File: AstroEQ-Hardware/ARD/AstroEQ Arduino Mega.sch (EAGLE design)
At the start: 19 parts, among them J1 POWER_JACKPTH, M0 Motor Driver, M1 Motor Driver

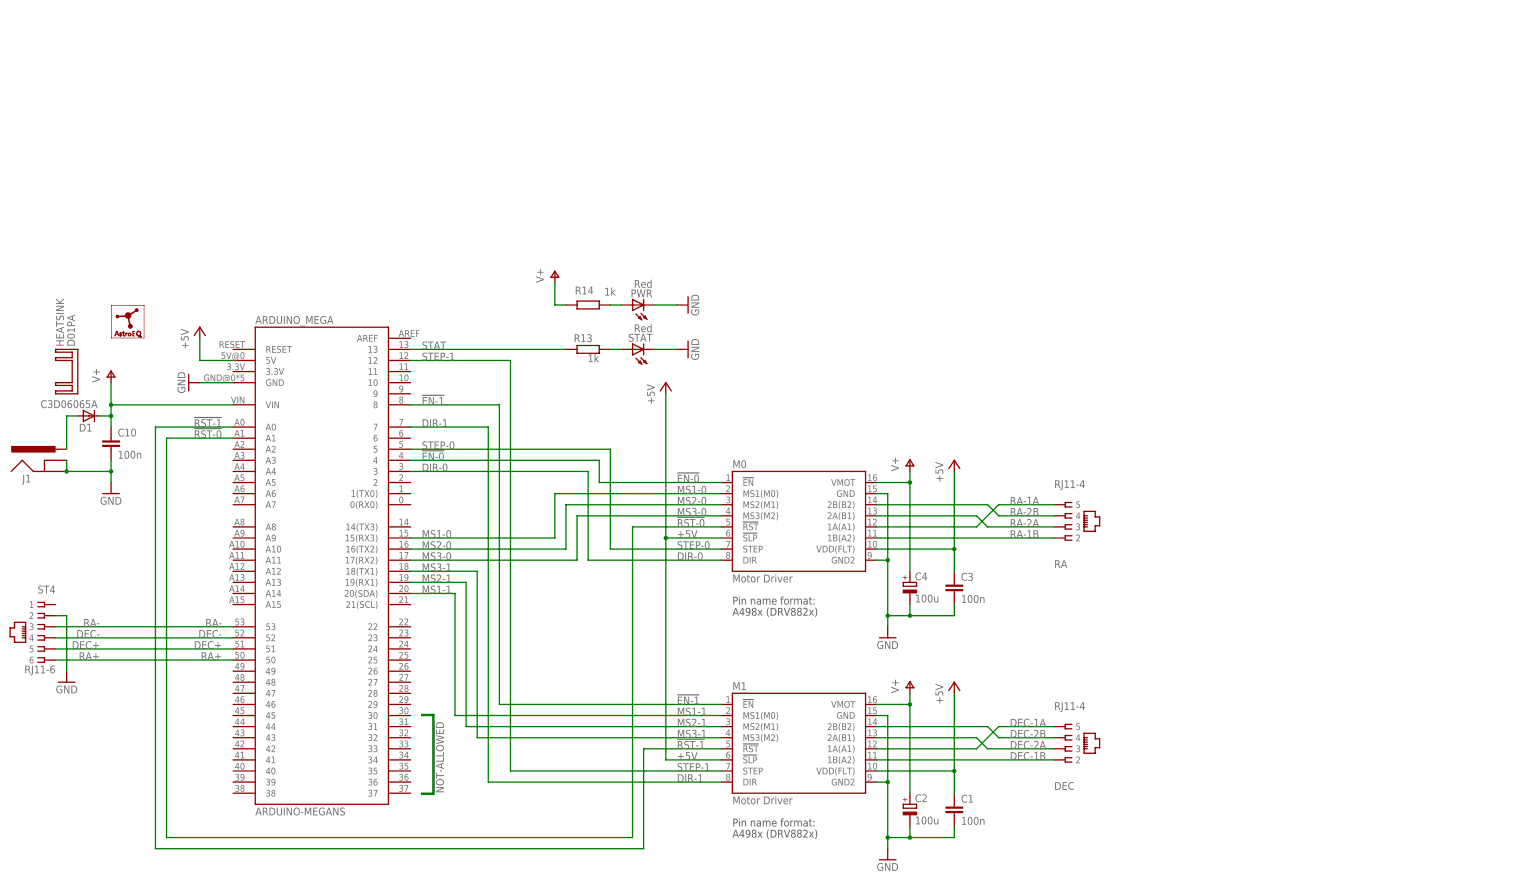
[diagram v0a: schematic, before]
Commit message: Update Arduino Mega PCB design to V4.8
Adds:
* Speed control line to ST4 connector
* DRV8834 support using 3-pin jumper selection headers.
* PWM output connector jack
* IO header for target speed selection, emergency stop, and snap pin.
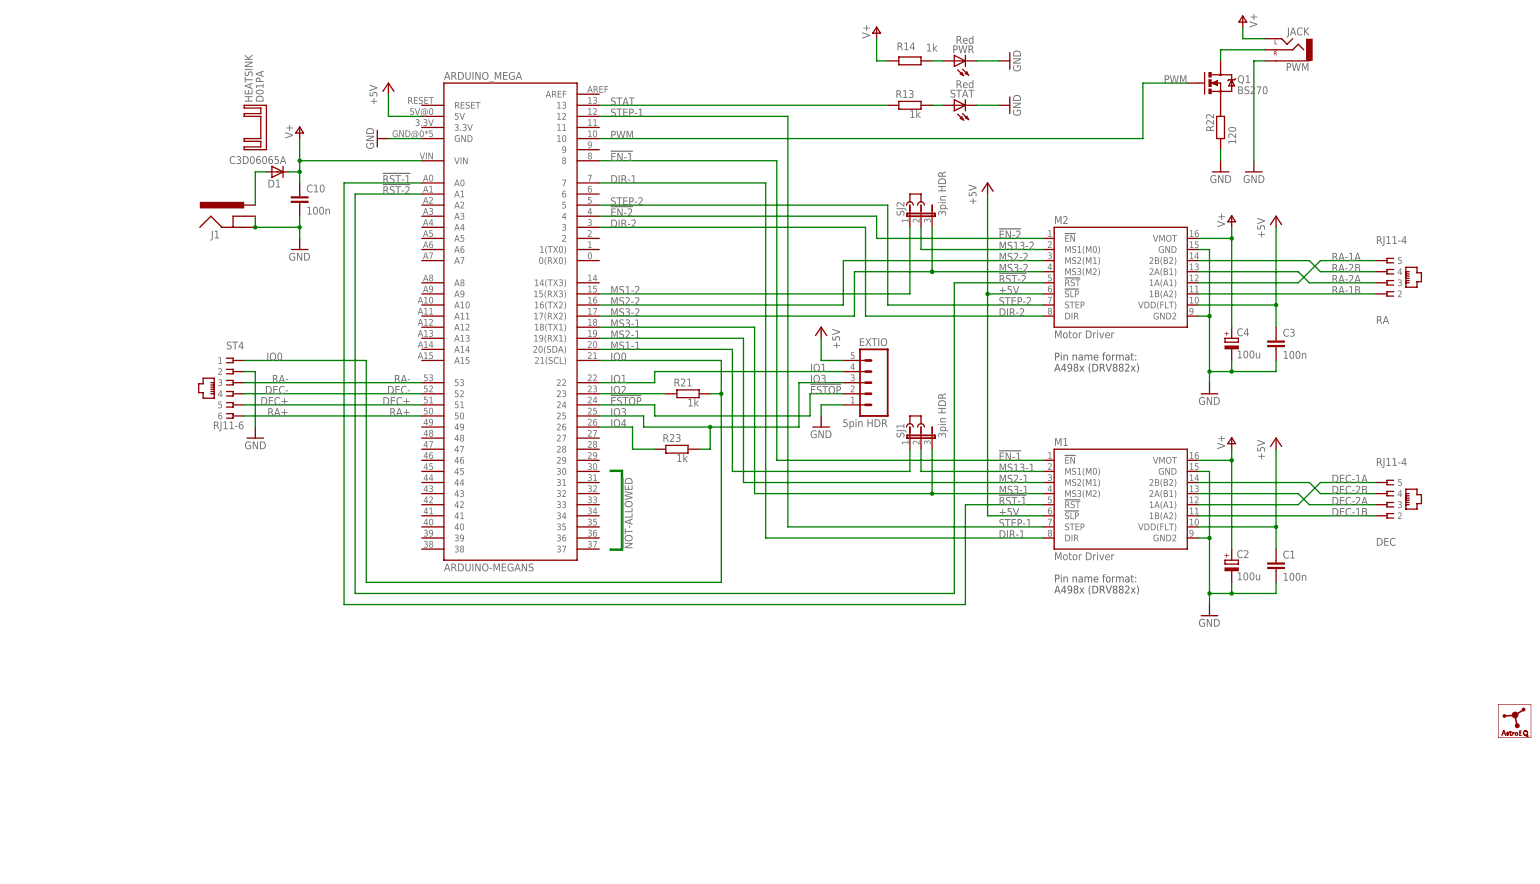
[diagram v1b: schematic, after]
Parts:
- removed M0: Motor Driver, A4983Carrier:A4983CARRIER
- added EXTIO: 5pin HDR, SparkFun:M05PTH
- added J2, J3: DNI, jumper:JUMPER
- added M2: Motor Driver, A4983Carrier:A4983CARRIER
- added PWM: JACK, SparkFun:AUDIO-JACKVERT
- added Q1: BS270, SparkFun:MOSFET-NCHANNELPTH
- added R21, R23: 1k, rcl:R-EU_0204/7
- added R22: 120, rcl:R-EU_0204/7
- added SJ1, SJ2: 3pin HDR, jumper:JP2E
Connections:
- removed net !EN-0: ARDUINO_MEGA.4, M0.!EN
- removed net !RST-0: ARDUINO_MEGA.A1, M0.!RST
- removed net DIR-0: ARDUINO_MEGA.3, M0.DIR
- removed net MS1-0: ARDUINO_MEGA.15(RX3), M0.MS1(M0)
- removed net MS2-0: ARDUINO_MEGA.16(TX2), M0.MS2(M1)
- removed net MS3-0: ARDUINO_MEGA.17(RX2), M0.MS3(M2)
- removed net STEP-0: ARDUINO_MEGA.5, M0.STEP
- new net !EN-2: ARDUINO_MEGA.4, M2.!EN
- new net !ESTOP: ARDUINO_MEGA.24, EXTIO.2
- new net !RST-2: ARDUINO_MEGA.A1, M2.!RST
- new net DIR-2: ARDUINO_MEGA.3, M2.DIR
- new net IO0: ARDUINO_MEGA.21(SCL), R21.2, ST4.1
- new net IO1: ARDUINO_MEGA.22, EXTIO.4
- new net IO2: ARDUINO_MEGA.23, R21.1
- new net IO3: ARDUINO_MEGA.25, EXTIO.3, R23.2
- new net IO4: ARDUINO_MEGA.26, R23.1
- new net MS1-2: ARDUINO_MEGA.15(RX3), SJ2.1
- new net MS13-1: M1.MS1(M0), SJ1.2
- new net MS13-2: M2.MS1(M0), SJ2.2
- new net MS2-2: ARDUINO_MEGA.16(TX2), M2.MS2(M1)
- new net MS3-2: ARDUINO_MEGA.17(RX2), M2.MS3(M2), SJ2.3
- new net PWM: ARDUINO_MEGA.10, Q1.G
- new net PWM-ILIM: Q1.S, R22.2
- new net PWM-OUT: PWM.RIGHT, Q1.D
- new net STEP-2: ARDUINO_MEGA.5, M2.STEP
- net +5V: now also EXTIO.5, M2.!SLP, M2.VDD(FLT); no longer M0.!SLP, M0.VDD(FLT)
- net GND: now also EXTIO.1, M2.GND, M2.GND2, PWM.SLEEVE, R22.1; no longer M0.GND, M0.GND2
- net MS1-1: now also SJ1.1; no longer M1.MS1(M0)
- net MS3-1: now also SJ1.3
- net RA-1A: now also M2.1A(A1); no longer M0.1A(A1)
- net RA-1B: now also M2.1B(A2); no longer M0.1B(A2)
- net RA-2A: now also M2.2A(B1); no longer M0.2A(B1)
- net RA-2B: now also M2.2B(B2); no longer M0.2B(B2)
- net V+: now also M2.VMOT, PWM.LEFT; no longer M0.VMOT
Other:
- moved on the sheet: ARDUINO_MEGA, C1, C10, C2, C3, C4, D1, DEC, HEATSINK, J1, M1, PWR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
